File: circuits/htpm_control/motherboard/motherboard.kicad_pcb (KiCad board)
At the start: 2 copper layers, 51 parts, among them J3 Conn_01x40_Socket, J5 Connector_Modcore, J6 Motor_Power, J7 Connector_Display, J8 Connector_Motor_Driver, U1 74HC165, U2 74HC165, U3 74HC165, U4 74HC165, U5 74HC595, U6 74HC595, U7 L7805

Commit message: Created HTPm CONTROL Motherboard PCB.
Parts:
- R1, R10, R11, R12, R13, R14, R15, R16, R17, R18, R19, R2, R20, R21, R22, R23, R24, R25, R26, R27, R28, R29, R3, R30, R4, R5, R6, R7, R8, R9: value 10kΩ -> 4.7kΩ
- moved J1 93.4 mm to (141.6, 90.8), turned to -90 degrees
- moved U1 89.8 mm to (80.6, 51.4), turned to 90 degrees
- moved J2 88.3 mm to (141.6, 85.7), turned to -90 degrees
- moved C5 77.4 mm to (71.8, 32.0), turned to -90 degrees
- moved J4 72.1 mm to (141.6, 71.8)
- moved C2 61.2 mm to (102.6, 38.7), turned to 180 degrees
- moved C6 60.2 mm to (71.8, 56.2), turned to -90 degrees
- moved R16 59.4 mm to (116.2, 55.5), turned to 90 degrees
- moved J5 59.2 mm to (141.6, 28.6)
- moved J3 58.0 mm to (88.3, 31.1), turned to -90 degrees
- moved R12 57.5 mm to (108.6, 39.7), turned to -90 degrees
- moved R11 55.9 mm to (111.1, 39.7), turned to -90 degrees
- moved R15 55.2 mm to (113.7, 55.5), turned to 90 degrees
- moved C4 54.9 mm to (102.6, 60.3), turned to 180 degrees
- moved R10 54.7 mm to (113.7, 39.7), turned to -90 degrees
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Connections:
- J1 pad 2: Net-(J1-GND) -> GND
- J3 pad 6: Net-(J1-GND) -> GND
- J4 pad 1: Net-(J1-GND) -> GND
- J5 pad 2: Net-(J1-GND) -> GND
- J7 pad 6: Net-(J1-GND) -> GND
- U7 pad 2: Net-(J1-GND) -> GND
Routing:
- net GND: track 0.00 -> 389.9 mm, vias 0 -> 9
- net Net-(J7-5V): track 0.00 -> 276.5 mm, vias 0 -> 1
- net Net-(J2-TIME_SET_DT): track 0.00 -> 181.4 mm, vias 0 -> 3
- net Net-(J5-VA): track 0.00 -> 169.5 mm
- net Net-(J5-VB): track 0.00 -> 167.0 mm
- net Net-(J2-TIME_SET_CLK): track 0.00 -> 165.8 mm, vias 0 -> 3
- net Net-(J3-GPIO12(PWM0)): track 0.00 -> 153.0 mm, vias 0 -> 2
- net Net-(J1-BIT_0): track 0.00 -> 143.0 mm, vias 0 -> 1
- net Net-(J2-11_LED): track 0.00 -> 142.5 mm, vias 0 -> 3
- net Net-(J2-13_LED): track 0.00 -> 137.2 mm, vias 0 -> 1
- net Net-(J1-BIT_1): track 0.00 -> 136.1 mm, vias 0 -> 1
- net Net-(J3-GPIO13(PWM1)): track 0.00 -> 135.0 mm, vias 0 -> 8
- net Net-(J3-GPIO23): track 0.00 -> 133.4 mm
- net Net-(J2-02_LED): track 0.00 -> 132.1 mm, vias 0 -> 3
- net Net-(J2-12_LED): track 0.00 -> 131.2 mm, vias 0 -> 2
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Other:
- board outline added: 90.2 x 71.1 mm
- board text added: "DISPLAY"
- board text added: "HTP!m CONTROL Motherboard by shawnd.xyz"
- board text added: "JLCJLCJLCJLC"
- board text added: "MD CONTROL"
- board text added: "MD POWER"
- board text added: "MODCORE"
- board text added: "PI HEADERS"
- board text added: "POWER"

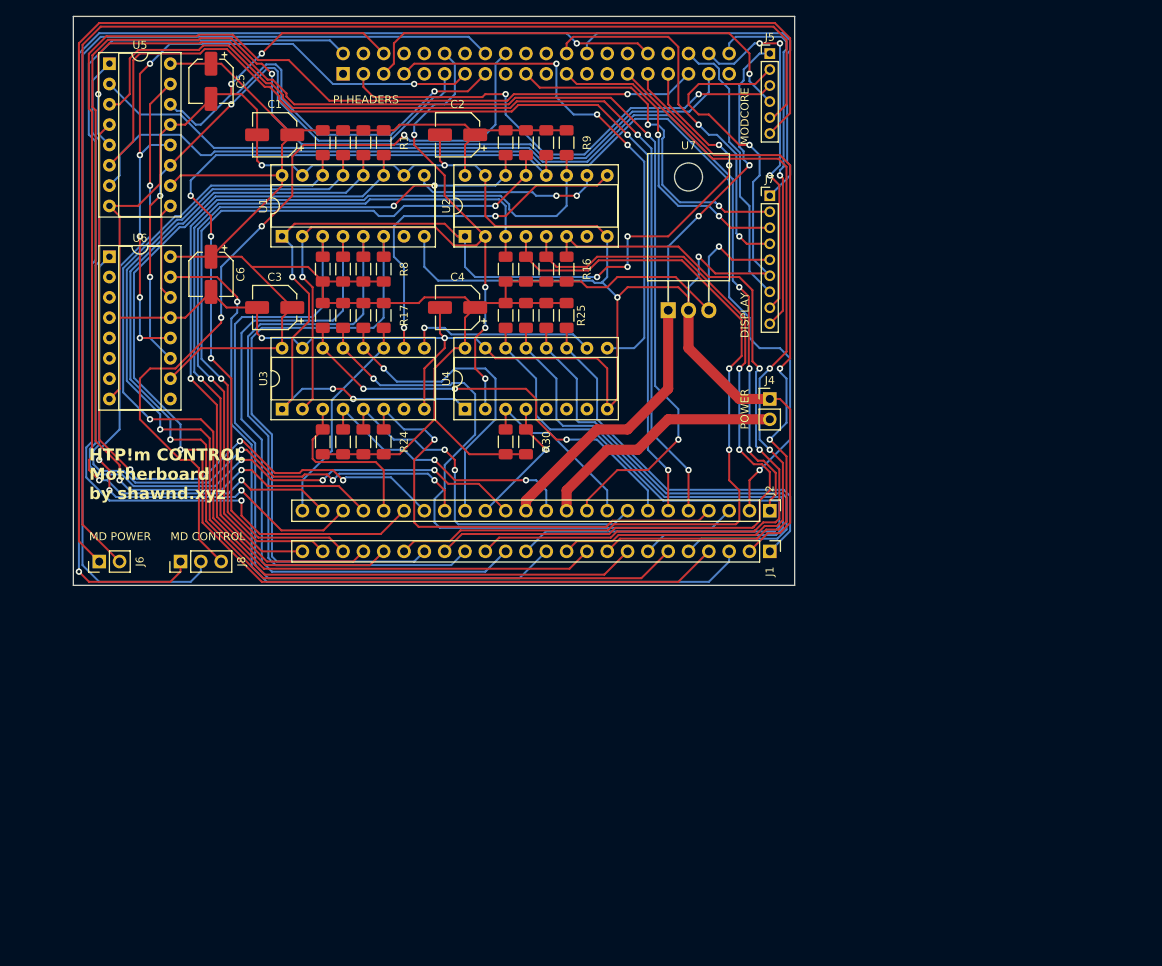
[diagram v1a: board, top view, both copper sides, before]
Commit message: Changed paper size.
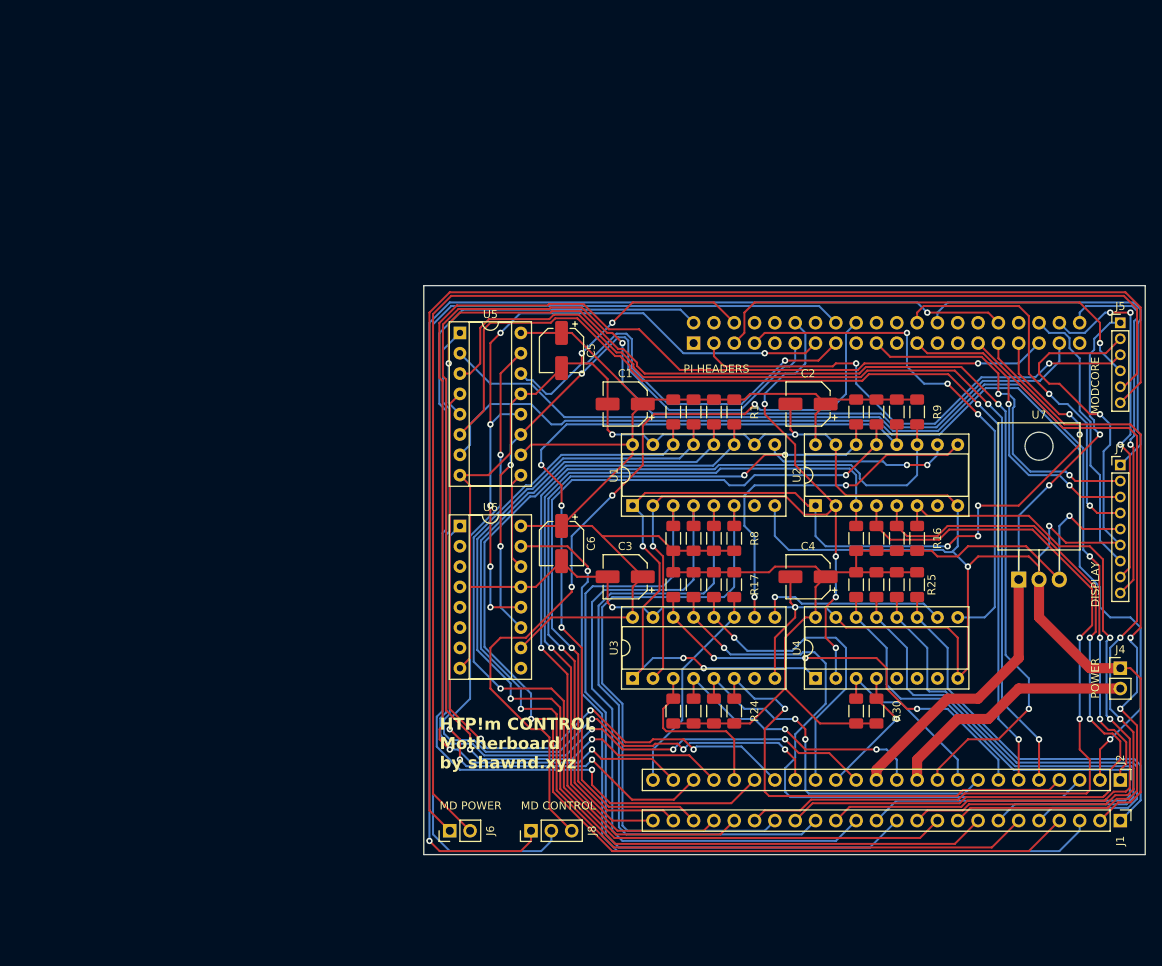
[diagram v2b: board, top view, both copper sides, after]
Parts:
- moved J3 55.2 mm to (132.1, 64.8)
- moved J8 55.2 mm to (111.8, 125.7)
- moved R13 55.2 mm to (152.4, 89.2)
- moved R16 55.2 mm to (160.0, 89.2)
- moved R19 55.2 mm to (132.1, 95.0)
- moved R22 55.2 mm to (132.1, 110.8)
- moved R25 55.2 mm to (160.0, 95.0)
- moved R28 55.2 mm to (152.4, 95.0)
- moved R29 55.2 mm to (152.4, 110.8)
- moved R6 55.2 mm to (132.1, 89.2)
- moved J7 55.2 mm to (185.4, 80.0)
- moved R12 55.2 mm to (152.4, 73.4)
- moved R14 55.2 mm to (154.9, 89.2)
- moved R3 55.2 mm to (132.1, 73.4)
- moved R5 55.2 mm to (129.5, 89.2)
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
